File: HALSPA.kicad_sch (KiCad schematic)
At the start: 71 parts, among them U1 HALSPA

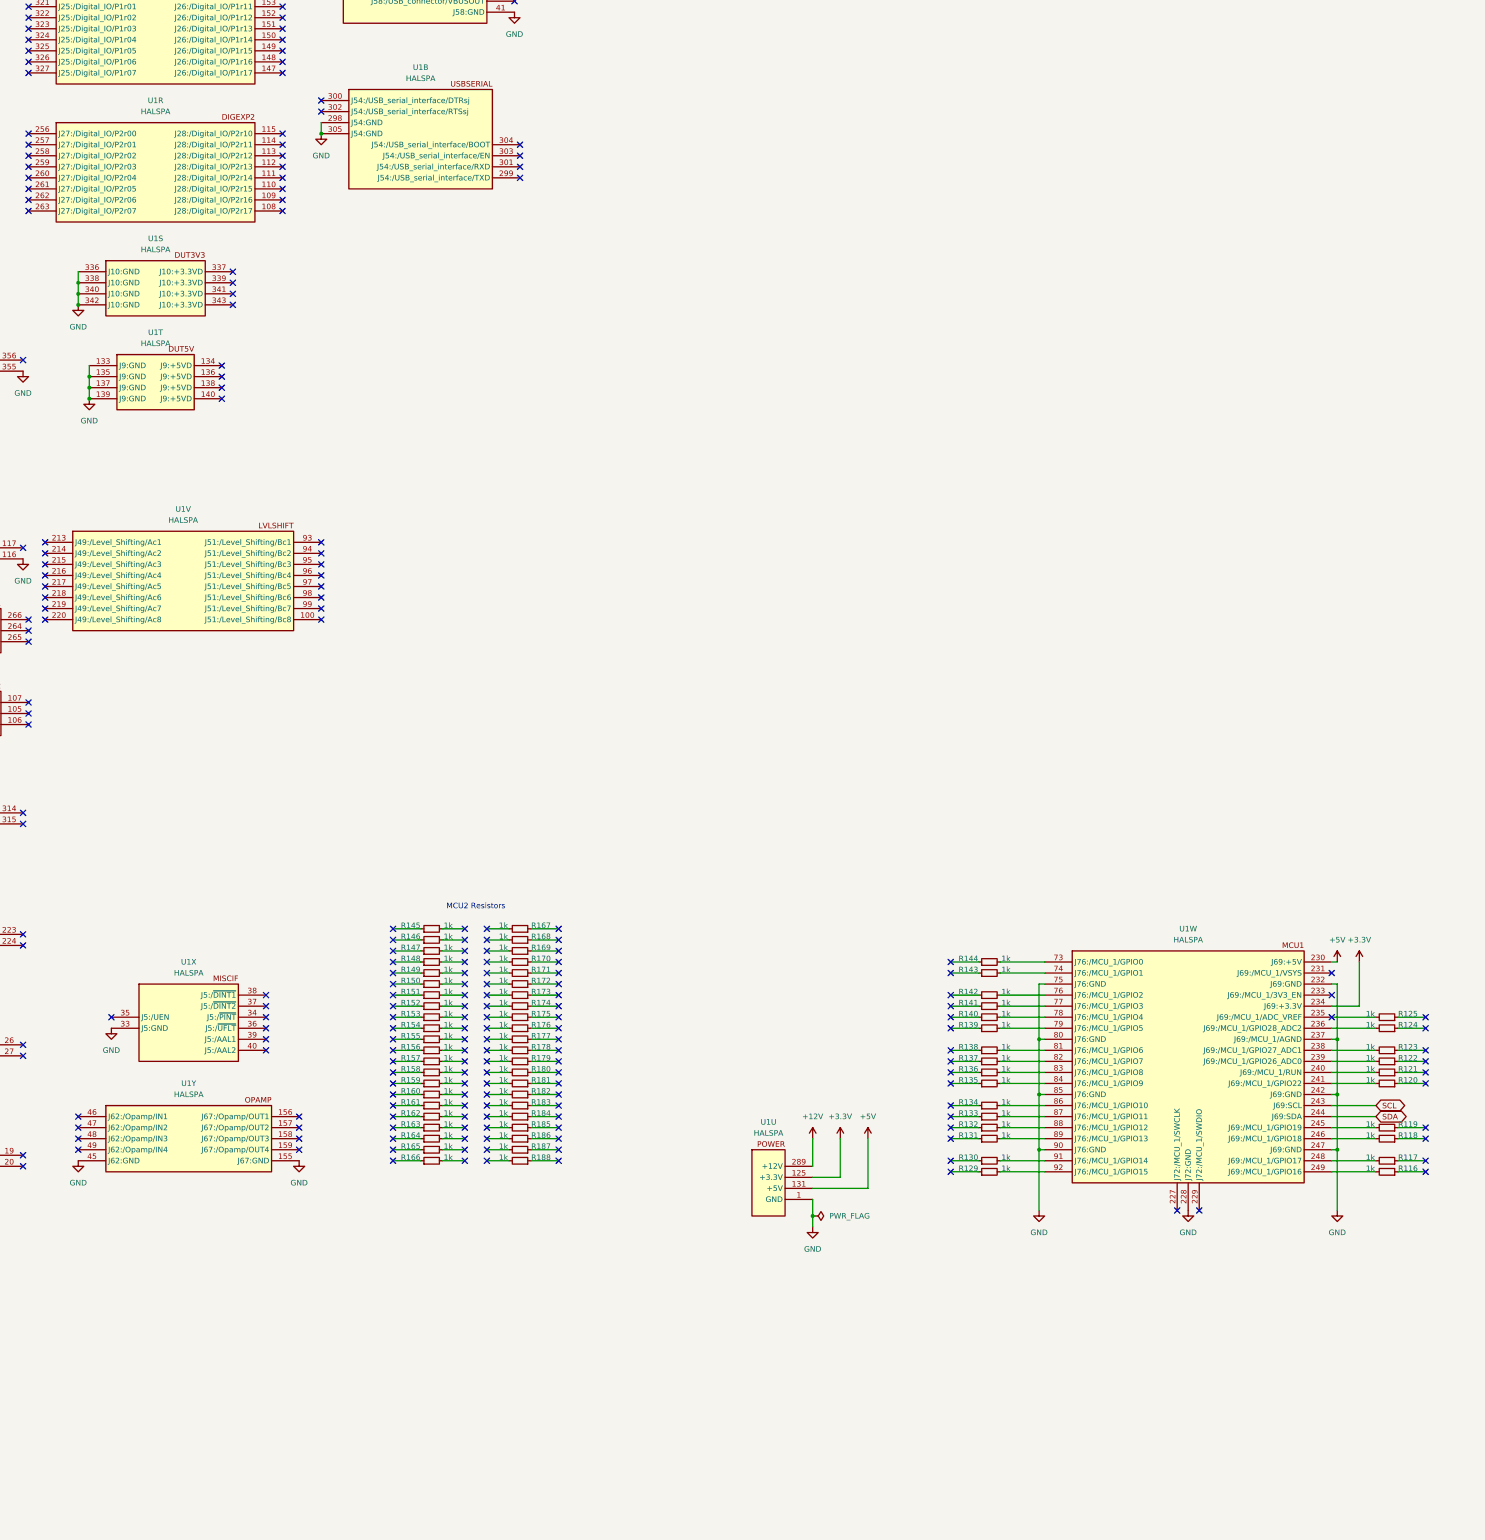
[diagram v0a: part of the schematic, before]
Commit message: Add MCU vertical headers
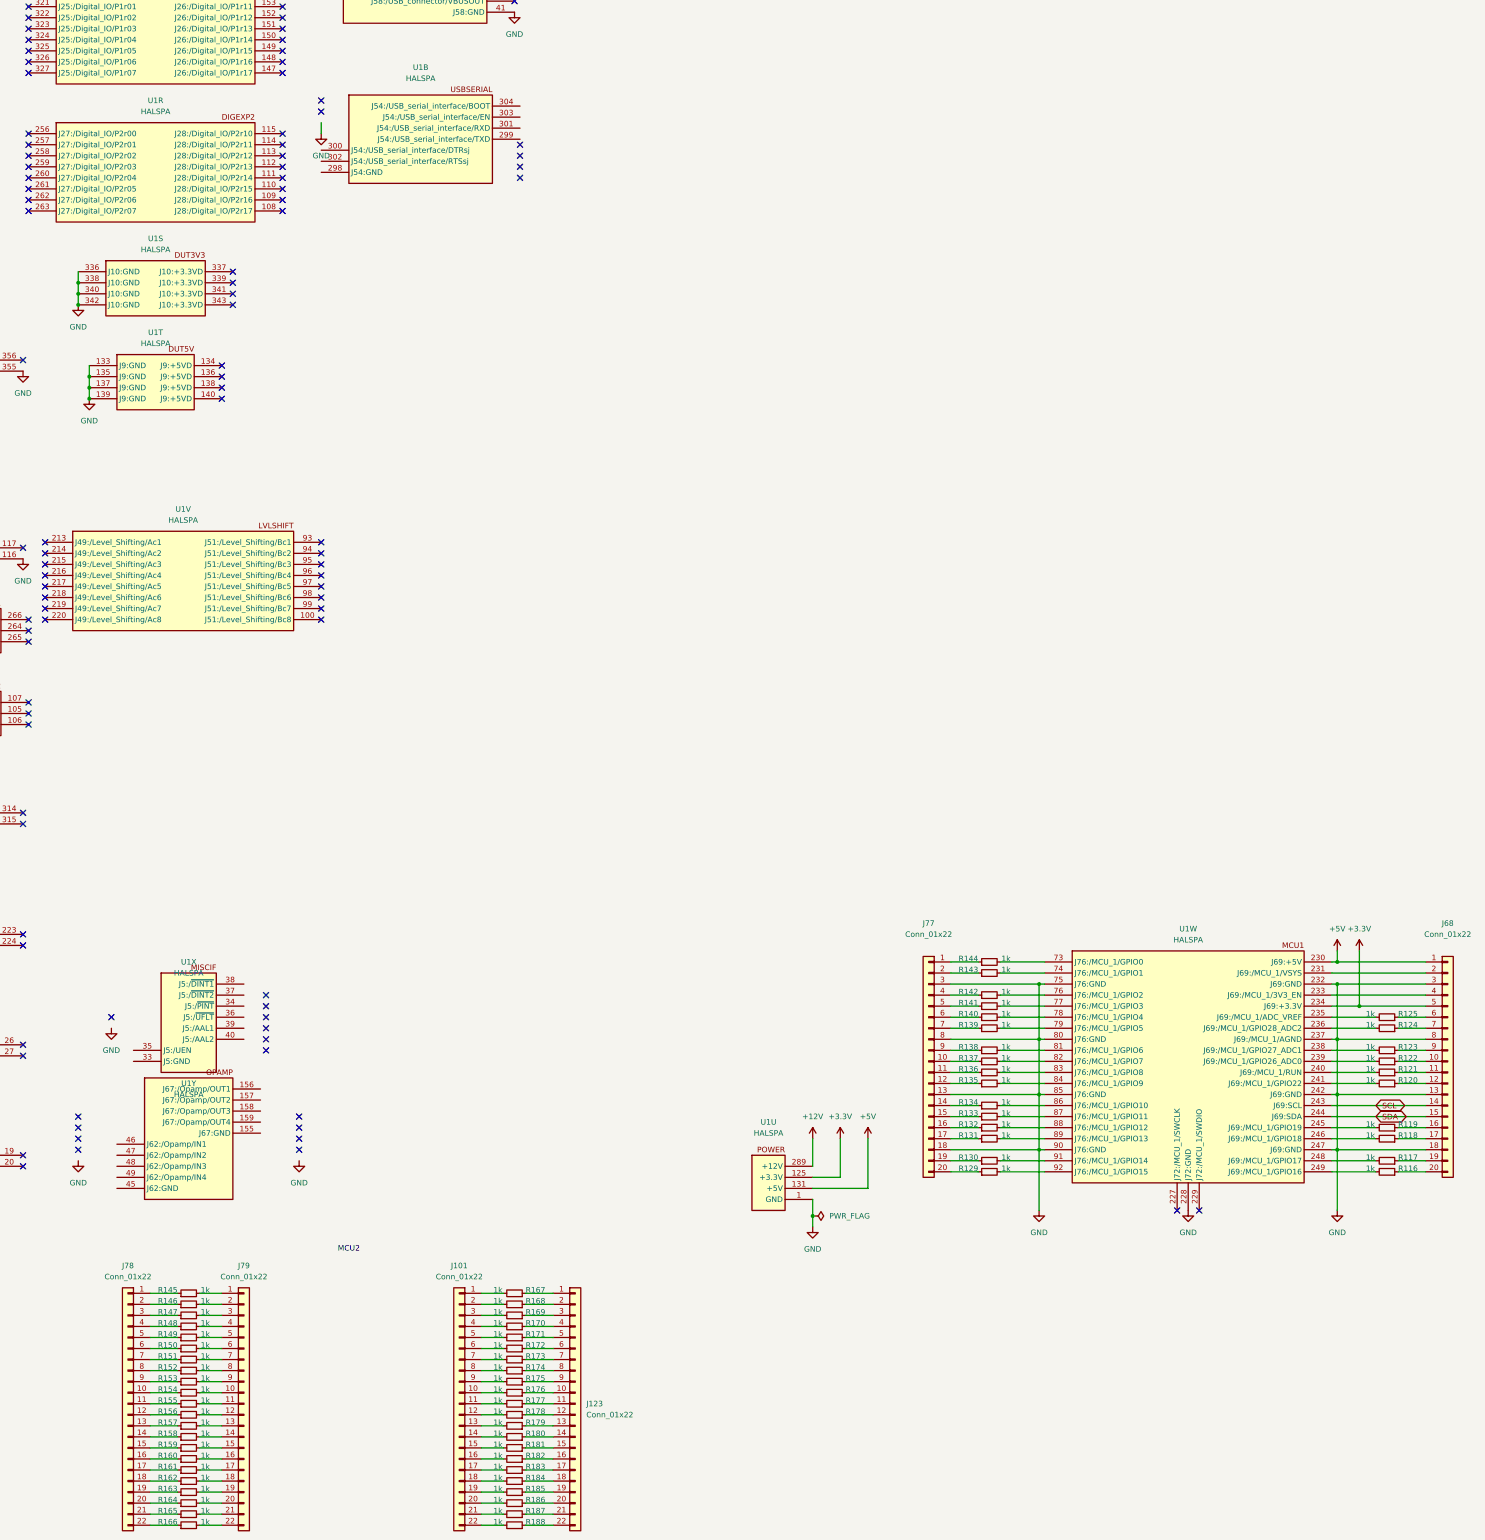
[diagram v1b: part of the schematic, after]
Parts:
- added J101, J123, J78, J79: Conn_01x22, HL_Connector_Pad_2.54mm:Pad_1x22_P2.54_1.7x1.7_Oct, symbol Connector_Generic:Conn_01x22
- added J68, J77: Conn_01x22, HL_Connector_Pad_2.54mm:Pad_1x22_P2.54_1.7x1.7_Oct, symbol Connector_Generic:Conn_01x20
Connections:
- net +3.3V: now also J68.5 (Pin_5)
- net +5V: now also J68.1 (Pin_1)
- net GND: now also J68.13 (Pin_13), J68.18 (Pin_18), J68.3 (Pin_3), J68.8 (Pin_8), J77.13 (Pin_13), J77.18 (Pin_18), J77.3 (Pin_3), J77.8 (Pin_8); no longer U1.155 (J67:GND), U1.298 (J54:GND), U1.305 (J54:GND), U1.33 (J5:GND), U1.45 (J62:GND)
- net SCL: now also J68.14 (Pin_14)
- net SDA: now also J68.15 (Pin_15)
- net at R155.1: now also J78.11 (Pin_11)
- net at R155.2: now also J79.11 (Pin_11)
- net at R175.1: now also J123.9 (Pin_9)
- net at R175.2: now also J101.9 (Pin_9)
- net at R132.1: now also J77.16 (Pin_16)
- net at R144.1: now also J77.1 (Pin_1)
- net at R116.1: now also J68.20 (Pin_20)
- net at R166.1: now also J78.22 (Pin_22)
- net at R166.2: now also J79.22 (Pin_22)
- net at R165.1: now also J78.21 (Pin_21)
- net at R165.2: now also J79.21 (Pin_21)
- net at R182.1: now also J123.16 (Pin_16)
- net at R182.2: now also J101.16 (Pin_16)
- net at R124.1: now also J68.7 (Pin_7)
- net at R162.1: now also J78.18 (Pin_18)
- net at R162.2: now also J79.18 (Pin_18)
- net at R178.1: now also J123.12 (Pin_12)
- net at R178.2: now also J101.12 (Pin_12)
- net at R184.1: now also J123.18 (Pin_18)
- net at R184.2: now also J101.18 (Pin_18)
- net at R119.1: now also J68.16 (Pin_16)
- net at R168.1: now also J123.2 (Pin_2)
- net at R168.2: now also J101.2 (Pin_2)
- net at R187.1: now also J123.21 (Pin_21)
- net at R187.2: now also J101.21 (Pin_21)
- net at R129.1: now also J77.20 (Pin_20)
- net at R149.1: now also J78.5 (Pin_5)
- net at R149.2: now also J79.5 (Pin_5)
- net at R179.1: now also J123.13 (Pin_13)
- net at R179.2: now also J101.13 (Pin_13)
- net at R117.1: now also J68.19 (Pin_19)
- net at R169.1: now also J123.3 (Pin_3)
- net at R169.2: now also J101.3 (Pin_3)
- net at R125.1: now also J68.6 (Pin_6)
- net at R159.1: now also J78.15 (Pin_15)
- net at R159.2: now also J79.15 (Pin_15)
- net at R163.1: now also J78.19 (Pin_19)
- net at R163.2: now also J79.19 (Pin_19)
- net at R167.1: now also J123.1 (Pin_1)
- net at R167.2: now also J101.1 (Pin_1)
- net at R143.1: now also J77.2 (Pin_2)
- net at R120.1: now also J68.12 (Pin_12)
- net at R145.1: now also J78.1 (Pin_1)
- net at R145.2: now also J79.1 (Pin_1)
- net at R164.1: now also J78.20 (Pin_20)
- net at R164.2: now also J79.20 (Pin_20)
- net at R185.1: now also J123.19 (Pin_19)
- net at R185.2: now also J101.19 (Pin_19)
- net at R138.1: now also J77.9 (Pin_9)
- net at R137.1: now also J77.10 (Pin_10)
- net at R183.1: now also J123.17 (Pin_17)
- net at R183.2: now also J101.17 (Pin_17)
- net at R140.1: now also J77.6 (Pin_6)
- net at R157.1: now also J78.13 (Pin_13)
- net at R157.2: now also J79.13 (Pin_13)
- net at R131.1: now also J77.17 (Pin_17)
- net at R186.1: now also J123.20 (Pin_20)
- net at R186.2: now also J101.20 (Pin_20)
- net at R136.1: now also J77.11 (Pin_11)
- net at R142.1: now also J77.4 (Pin_4)
- net at R171.1: now also J123.5 (Pin_5)
- net at R171.2: now also J101.5 (Pin_5)
- net at R172.1: now also J123.6 (Pin_6)
- net at R172.2: now also J101.6 (Pin_6)
- net at R180.1: now also J123.14 (Pin_14)
- net at R180.2: now also J101.14 (Pin_14)
- net at R134.1: now also J77.14 (Pin_14)
- net at R122.1: now also J68.10 (Pin_10)
- net at R150.1: now also J78.6 (Pin_6)
- net at R150.2: now also J79.6 (Pin_6)
- net at R161.1: now also J78.17 (Pin_17)
- net at R161.2: now also J79.17 (Pin_17)
- net at R118.1: now also J68.17 (Pin_17)
- net at R181.1: now also J123.15 (Pin_15)
- net at R181.2: now also J101.15 (Pin_15)
- net at R148.1: now also J78.4 (Pin_4)
- net at R148.2: now also J79.4 (Pin_4)
- net at R141.1: now also J77.5 (Pin_5)
- net at R176.1: now also J123.10 (Pin_10)
- net at R176.2: now also J101.10 (Pin_10)
- net at R151.1: now also J78.7 (Pin_7)
- net at R151.2: now also J79.7 (Pin_7)
- net at R177.1: now also J123.11 (Pin_11)
- net at R177.2: now also J101.11 (Pin_11)
- net at R123.1: now also J68.9 (Pin_9)
- net at R154.1: now also J78.10 (Pin_10)
- net at R154.2: now also J79.10 (Pin_10)
- net at R130.1: now also J77.19 (Pin_19)
- net at R153.1: now also J78.9 (Pin_9)
- net at R153.2: now also J79.9 (Pin_9)
- net at R139.1: now also J77.7 (Pin_7)
- net at R135.1: now also J77.12 (Pin_12)
- net at R146.1: now also J78.2 (Pin_2)
- net at R146.2: now also J79.2 (Pin_2)
- net at R188.1: now also J123.22 (Pin_22)
- net at R188.2: now also J101.22 (Pin_22)
- net at R173.1: now also J123.7 (Pin_7)
- net at R173.2: now also J101.7 (Pin_7)
- net at R133.1: now also J77.15 (Pin_15)
- net at R121.1: now also J68.11 (Pin_11)
- net at R158.1: now also J78.14 (Pin_14)
- net at R158.2: now also J79.14 (Pin_14)
- net at R170.1: now also J123.4 (Pin_4)
- net at R170.2: now also J101.4 (Pin_4)
- net at R156.1: now also J78.12 (Pin_12)
- net at R156.2: now also J79.12 (Pin_12)
- net at U1.231 (J69:/MCU_1/VSYS): now also J68.2 (Pin_2)
- net at U1.233 (J69:/MCU_1/3V3_EN): now also J68.4 (Pin_4)
- net at R174.1: now also J123.8 (Pin_8)
- net at R174.2: now also J101.8 (Pin_8)
- net at R152.1: now also J78.8 (Pin_8)
- net at R152.2: now also J79.8 (Pin_8)
- net at R147.1: now also J78.3 (Pin_3)
- net at R147.2: now also J79.3 (Pin_3)
- net at R160.1: now also J78.16 (Pin_16)
- net at R160.2: now also J79.16 (Pin_16)
- new net J54:GND: U1.298 (J54:GND), U1.305 (J54:GND)
- no-connect marks 305 -> 188
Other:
- note added: "MCU2"
- note removed: "MCU2 Resistors"
